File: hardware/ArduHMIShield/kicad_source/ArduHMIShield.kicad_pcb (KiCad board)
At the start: 2 copper layers, 68.3 x 53 mm, 29 parts, among them CN1 ARDUINO, Q1 Q_NMOS_GSD, SW1 TAST_HOR, SW2 TAST_HOR, SW3 TAST_HOR, SW4 TAST_HOR, SW5 TAST_HOR, SW6 TAST_HOR

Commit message: reworked schematic and layout, both seem to be finished
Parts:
- added C10: C_0603, capacitors:C_0603, F.Cu at (112.3, 108.1)
- added C11: C_0603, capacitors:C_0603, F.Cu at (112.3, 106.4)
- added C12: C_0603, capacitors:C_0603, F.Cu at (71.0, 87.6)
- added C13: C_0603, capacitors:C_0603, F.Cu at (77.5, 87.6)
- added C14: C_0603, capacitors:C_0603, F.Cu at (84.1, 87.6)
- added IC1: SN74LVC2G34, SOT_TO:SOT-23-6, F.Cu at (84.1, 90.5)
- added IC2: SN74LVC2G34, SOT_TO:SOT-23-6, F.Cu at (77.5, 90.5)
- added IC3: SN74LVC2G34, SOT_TO:SOT-23-6, F.Cu at (71.0, 90.5)
- added R10: 1k, resistors:R_0603, F.Cu at (81.6, 90.4)
- added R11: 1k, resistors:R_0603, F.Cu at (79.9, 90.4)
- added R12: 1k, resistors:R_0603, F.Cu at (75.1, 90.4)
- added R13: 1k, resistors:R_0603, F.Cu at (68.6, 90.4)
- added R14: 1k, resistors:R_0603, F.Cu at (73.4, 90.4)
- added R15: 1k, resistors:R_0603, F.Cu at (79.9, 94.3)
- added R16: 1k, resistors:R_0603, F.Cu at (70.5, 94.3)
- added R17: 1k, resistors:R_0603, F.Cu at (83.3, 94.3)
- added R18: 1k, resistors:R_0603, F.Cu at (78.2, 94.3)
- added R19: 1k, resistors:R_0603, F.Cu at (68.8, 94.3)
- added R20: 1k, resistors:R_0603, F.Cu at (81.6, 94.3)
- added U1: LT1117, SOT_TO:SOT-223, F.Cu at (113.3, 100.5)
- moved R2 55.9 mm to (65.3, 93.0), turned to 90 degrees
- moved R3 49.8 mm to (53.1, 90.1), turned to 270 degrees
- moved R4 48.6 mm to (54.3, 116.4), turned to 180 degrees
- moved SW2 35.5 mm to (59.0, 90.0)
- moved R9 32.0 mm to (107.8, 120.4)
- moved R1 22.3 mm to (82.7, 122.1), turned to 90 degrees
- moved R5 20.8 mm to (54.3, 118.6)
- moved SW5 13.4 mm to (59.0, 125.0)
- moved SW4 9.33 mm to (55.0, 100.0), turned to 180 degrees
- moved R8 8.89 mm to (114.0, 121.1), turned to 90 degrees
- moved SW3 8.89 mm to (59.0, 110.0), turned to 270 degrees
- moved R7 6.23 mm to (115.8, 121.0), turned to 90 degrees
- moved SW1 5.58 mm to (63.0, 100.0)
- moved Q1 5.02 mm to (110.8, 120.3)
- moved R6 3.50 mm to (117.6, 121.0), turned to 90 degrees
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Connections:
- net /DISPLAY_D4 renamed Net-(CN1-Pad4)
- net Net-(R2-Pad2) renamed /BUTTON_UP
- net Net-(R3-Pad2) renamed /BUTTON_DOWN
- net Net-(R4-Pad2) renamed /BUTTON_LEFT
- net Net-(R5-Pad2) renamed /BUTTON_SELECT
- CN1 pad 11: Net-(CN1-Pad11) -> /ARDU_SI_1
- CN1 pad 12: Net-(CN1-Pad12) -> /ARDU_CS_1
- CN1 pad 13: Net-(CN1-Pad13) -> /ARDU_CLK_1
- CN1 pad 5: /DISPLAY_D5 -> /ARDU_SI_2
- CN1 pad 6: /DISPLAY_D6 -> /ARDU_CS_2
- CN1 pad 7: /DISPLAY_D7 -> /ARDU_CLK_2
- CN1 pad 8: /DISPLAY_RS -> /ARDU_A0
- CN1 pad 9: /DISPLAY_E -> /ARDU_RESET
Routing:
- net GND: track 5.08 -> 264.9 mm, vias 0 -> 8
- net +5V: track 0.36 -> 115.7 mm, vias 0 -> 1
- net +3V3: track 7.62 -> 76.9 mm, vias 0 -> 2
- net /RESET: track 0.00 -> 63.9 mm, vias 0 -> 1
- net /DIS_C1: track 0.00 -> 63.7 mm, vias 0 -> 1
- net /KEYPAD_A0: track 4.12 -> 67.7 mm
- net /DISPLAY_BL: track 0.00 -> 56.4 mm
- net /ARDU_CS_2: track 0.00 -> 48.1 mm, vias 0 -> 1
- net /ARDU_A0: track 0.00 -> 43.0 mm, vias 0 -> 1
- net /BUTTON_DOWN: track 0.00 -> 42.7 mm
- net /ARDU_SI_2: track 0.00 -> 41.4 mm, vias 0 -> 1
- net /ARDU_RESET: track 0.00 -> 39.3 mm, vias 0 -> 1
- net /ARDU_CLK_2: track 0.00 -> 38.6 mm, vias 0 -> 1
- net /DIS_C2: track 0.00 -> 35.9 mm, vias 0 -> 1
- net /ARDU_CS_1: track 0.00 -> 35.4 mm, vias 0 -> 1
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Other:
- board size 68.3 x 53 mm -> 72 x 53 mm

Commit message: updated schematic and layout
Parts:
- added R21: 1k, resistors:R_0603, F.Cu at (65.5, 123.0)
- C1, C10, C11, C2, C3, C4, C5, C6, C7, C8, C9: value C_0603 -> 1u
- C12, C13, C14: value C_0603 -> 100n
- R10, R11, R12, R13, R14, R15, R16, R17: value 1k -> DNI
- R18, R19, R20: value 1k -> 0R
- moved R18 10.2 mm to (87.4, 98.6), turned to 180 degrees
- moved R15 9.60 mm to (87.4, 100.3), turned to 180 degrees
- moved R19 9.11 mm to (77.8, 95.7), turned to 180 degrees
- moved R16 7.93 mm to (77.8, 97.4), turned to 180 degrees
- moved R20 5.87 mm to (87.4, 95.2), turned to 180 degrees
- moved R17 4.85 mm to (87.4, 96.9), turned to 180 degrees
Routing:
- net +3V3: track 76.9 -> 103.8 mm
- net /DIS_C1: track 63.7 -> 84.0 mm
- net GND: track 264.9 -> 279.3 mm, vias 8 -> 9
- net /ARDU_SI_2: track 41.4 -> 30.2 mm
- net /ARDU_CS_1: track 35.4 -> 24.4 mm
- net /ARDU_CS_2: track 48.1 -> 37.1 mm
- net /ARDU_CLK_2: track 38.6 -> 27.9 mm
- net /ARDU_CLK: track 5.74 -> 14.5 mm
- net /ARDU_SI_1: track 23.8 -> 17.3 mm
- net /ARDU_CS: track 6.65 -> 12.5 mm
- net Net-(Q1-Pad3): track 5.84 -> 11.6 mm
- net /ARDU_CLK_1: track 26.5 -> 21.8 mm
- net /ARDU_A0: track 43.0 -> 39.2 mm
- net /ARDU_SI: track 5.84 -> 9.32 mm
- net /RESET: track 63.9 -> 66.5 mm
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
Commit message: finished layout and generated output files
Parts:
- removed IC1, IC2, IC3: SN74LVC2G34, SOT_TO:SOT-23-6
- added D1: green, LEDs:LED_0603, F.Cu at (66.2, 124.7)
- added U2: TLV733P, SOT_TO:SOT-23-5, F.Cu at (118.9, 102.4)
- added U3: SN74LVC2G34, SOT_TO:SOT-23-6, F.Cu at (84.1, 90.5)
- added U4: SN74LVC2G34, SOT_TO:SOT-23-6, F.Cu at (77.5, 90.5)
- added U5: SN74LVC2G34, SOT_TO:SOT-23-6, F.Cu at (71.0, 90.5)
- moved R21 1.84 mm to (66.2, 121.3), turned to 90 degrees
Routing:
- net +3V3: track 103.8 -> 162.7 mm, vias 2 -> 4
- net GND: track 279.3 -> 302.4 mm, vias 9 -> 10
- net +5V: track 115.7 -> 118.3 mm, vias 1 -> 0
- net Net-(D1-Pad2): track 0.00 -> 1.90 mm
- net /ARDU_RESET: track 38.1 -> 38.6 mm
- net /DIS_C1: track 84.0 -> 84.6 mm

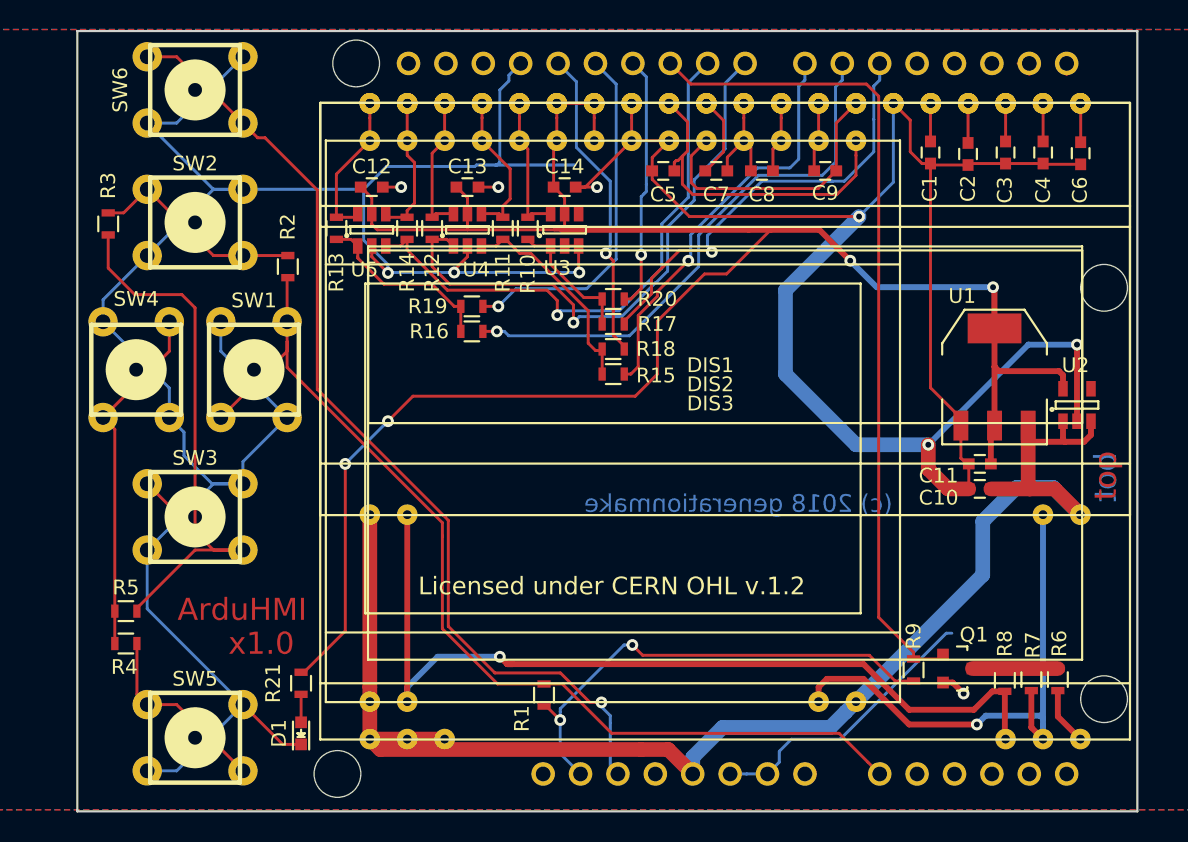
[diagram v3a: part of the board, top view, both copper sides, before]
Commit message: updated pcb and schematic to version 1.1, see changes in CHANGES.txt
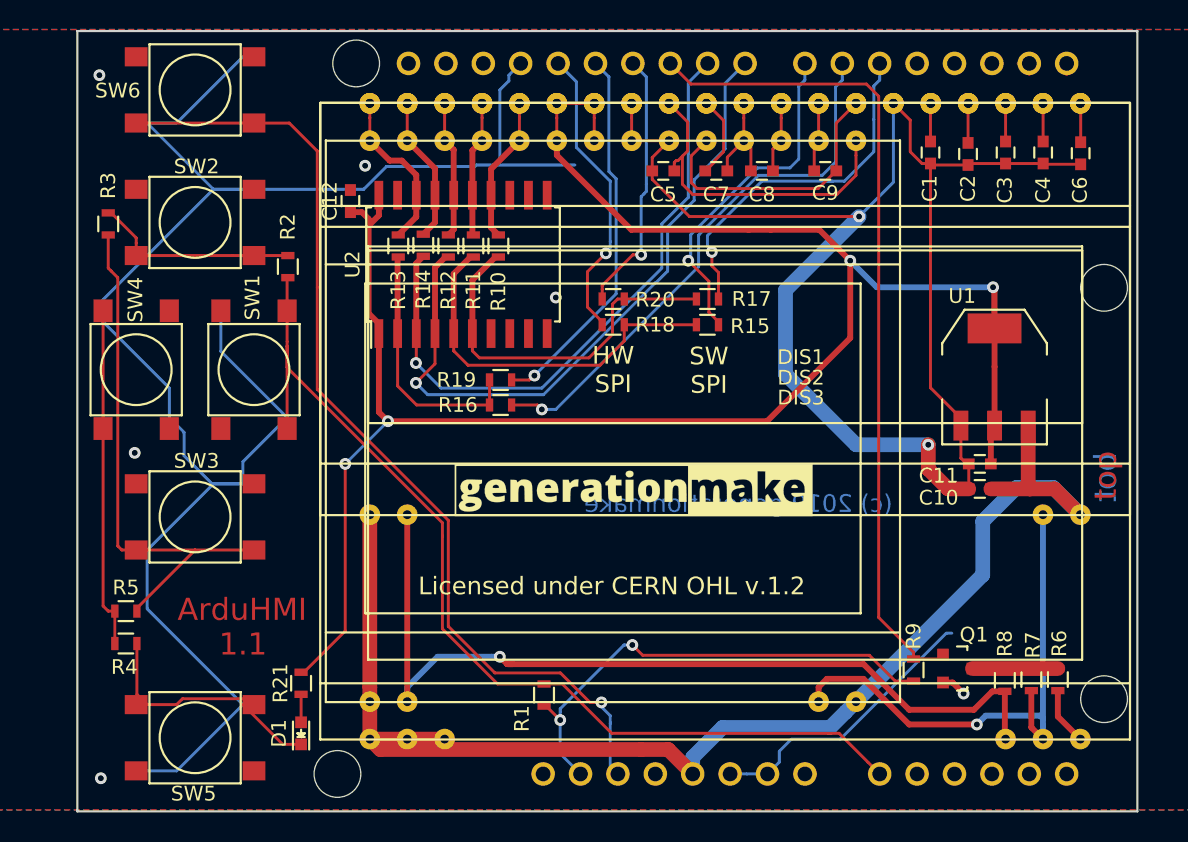
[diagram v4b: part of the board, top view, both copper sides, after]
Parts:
- removed C13, C14: 100n, capacitors:C_0603
- removed U3, U4, U5: SN74LVC2G34, SOT_TO:SOT-23-6
- added G***: generationmake_logo, labels:generationmake_logo, F.Cu at (88.8, 113.5)
- added G***: generationmake_logo, labels:generationmake_logo, B.Cu at (101.9, 105.5)
- Q1: value Q_NMOS_GSD -> 2N7002
- SW1, SW2, SW3, SW4, SW5, SW6: value TAST_HOR -> TAST_VER; footprint mechanical-switches:PCB_PUSH -> mechanical-switches:WE_430182050816
- U2: value TLV733P -> 74VHC245D; footprint SOT_TO:SOT-23-5 -> SOIC:SOIC-20_7.5x12.8mm_Pitch1.27mm
- moved U2 42.8 mm to (77.2, 92.8)
- moved R15 7.22 mm to (93.8, 97.0)
- moved R17 6.62 mm to (93.8, 95.2)
- moved R16 5.37 mm to (79.8, 102.4)
- moved R19 5.37 mm to (79.8, 100.7)
- moved R13 4.37 mm to (72.8, 91.6)
- moved R10 2.33 mm to (79.6, 91.6)
- moved R11 2.33 mm to (77.9, 91.6)
- moved C12 1.73 mm to (69.5, 88.5), turned to 90 degrees
- moved R18 1.65 mm to (87.4, 97.0), turned to 0 degrees
- moved R12 1.63 mm to (76.2, 91.6)
- moved R14 1.59 mm to (74.5, 91.5)
- turned R20 to 0 degrees
- turned SW1 to 90 degrees
- turned SW2 to 0 degrees
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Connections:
- CN1 pad 0: Net-(CN1-Pad0) -> (no net)
- CN1 pad 1: Net-(CN1-Pad1) -> (no net)
- CN1 pad 15: Net-(CN1-Pad15) -> (no net)
- CN1 pad 16: Net-(CN1-Pad16) -> (no net)
- CN1 pad 17: Net-(CN1-Pad17) -> (no net)
- CN1 pad 18: /ENC_SW -> (no net)
- CN1 pad 19: /ENC_B -> (no net)
- CN1 pad 2: Net-(CN1-Pad2) -> (no net)
- CN1 pad 20: /ENC_A -> (no net)
- CN1 pad 21: Net-(CN1-Pad21) -> (no net)
- CN1 pad 22: Net-(CN1-Pad22) -> (no net)
- CN1 pad 24: VIN -> (no net)
- CN1 pad 28: Net-(CN1-Pad28) -> (no net)
- CN1 pad 3: Net-(CN1-Pad3) -> (no net)
- CN1 pad 31: Net-(CN1-Pad31) -> (no net)
- CN1 pad 4: Net-(CN1-Pad4) -> (no net)
- SW1 pad 2: GND -> /KEYPAD_A0
- SW1 pad 3: /KEYPAD_A0 -> GND
- SW2 pad 2: GND -> /BUTTON_UP
- SW2 pad 3: /BUTTON_UP -> GND
- SW3 pad 2: GND -> /BUTTON_DOWN
- SW3 pad 3: /BUTTON_DOWN -> GND
- SW4 pad 2: GND -> /BUTTON_LEFT
- SW4 pad 3: /BUTTON_LEFT -> GND
- SW5 pad 2: GND -> /BUTTON_SELECT
- SW5 pad 3: /BUTTON_SELECT -> GND
- SW6 pad 2: GND -> /RESET
- SW6 pad 3: /RESET -> GND
- U2 pad 1: +5V -> +3V3
- U2 pad 2: GND -> /ARDU_CS
- U2 pad 3: +5V -> /ARDU_RESET
- U2 pad 4: Net-(U2-Pad4) -> /ARDU_A0
- U2 pad 5: +3V3 -> /ARDU_CLK
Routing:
- net GND: track 302.4 -> 248.6 mm, vias 10 -> 8
- net +3V3: track 162.7 -> 140.2 mm
- net /ARDU_SI: track 9.32 -> 25.5 mm
- net /ARDU_CLK: track 14.5 -> 25.7 mm
- net /ARDU_A0: track 39.5 -> 46.8 mm
- net /BUTTON_DOWN: track 42.7 -> 35.8 mm
- net +5V: track 118.3 -> 111.4 mm
- net /ARDU_SI_2: track 30.2 -> 24.9 mm
- net (no net): track 0.00 -> 5.07 mm
- net /ARDU_RESET: track 38.6 -> 43.4 mm
- net /ARDU_CS: track 12.5 -> 17.3 mm
- net /ARDU_CLK_2: track 27.9 -> 23.3 mm
- net Net-(CN1-Pad1): track 1.96 -> 0.00 mm
- net /ARDU_CS_1: track 24.4 -> 25.9 mm
- net /KEYPAD_A0: track 69.1 -> 67.7 mm
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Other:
- board text added: "(c) 2019 generationmake"
- board text added: "1.1"
- board text added: "Copyright generationmake 2019 see full project documentation at http://arduhmi.generationmake.de This documentation describes Open Hardware and is licensed under the CERN OHL v. 1.2. You may redistribute and modify this documentation under the terms of the CERN OHL v.1.2. (http://ohwr.org/cernohl). This documentation is distributed WITHOUT ANY EXPRESS OR IMPLIED WARRANTY, INCLUDING OF MERCHANTABI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"
- board text added: "HW SPI"
- board text added: "SW SPI"
- board text added: "for EA DOGS102-6 EA DOGM132-5 EA DOGM128-6"
- board text removed: "(c) 2018 generationmake"
- board text removed: "Copyright generationmake 2018 see full project documentation at http://ardutrx.generationmake.de This documentation describes Open Hardware and is licensed under the CERN OHL v. 1.2. You may redistribute and modify this documentation under the terms of the CERN OHL v.1.2. (http://ohwr.org/cernohl). This documentation is distributed WITHOUT ANY EXPRESS OR IMPLIED WARRANTY, INCLUDING OF MERCHANTABI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"
- board text removed: "x1.0"
